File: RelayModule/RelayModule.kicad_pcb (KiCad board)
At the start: 2 copper layers, 49.9 x 21.3 mm, 16 parts, among them P1 Control_connector, P2 Power_connector, Q1 S8050, U1 PC817

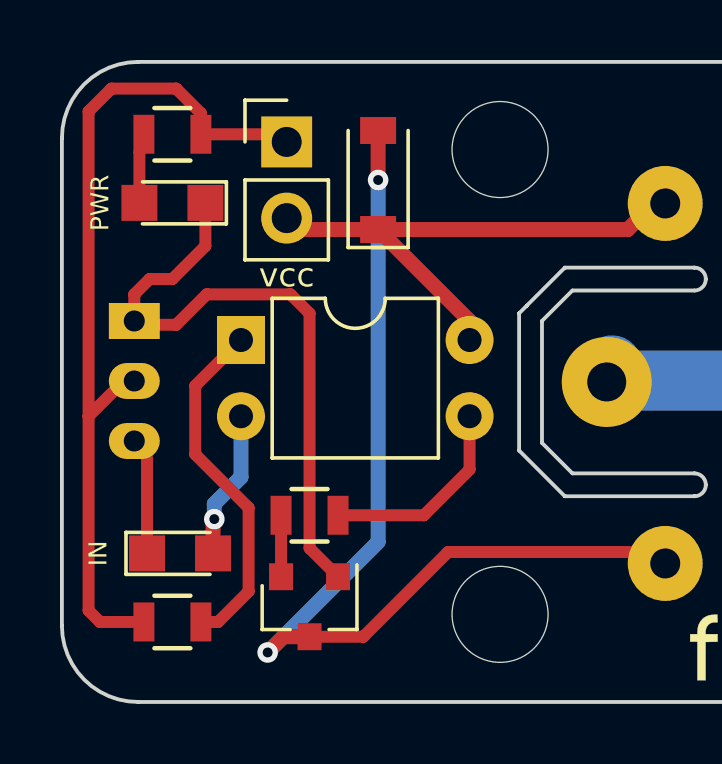
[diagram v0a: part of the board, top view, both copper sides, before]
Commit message: Solucionado un error en el footprint del transistor S8050
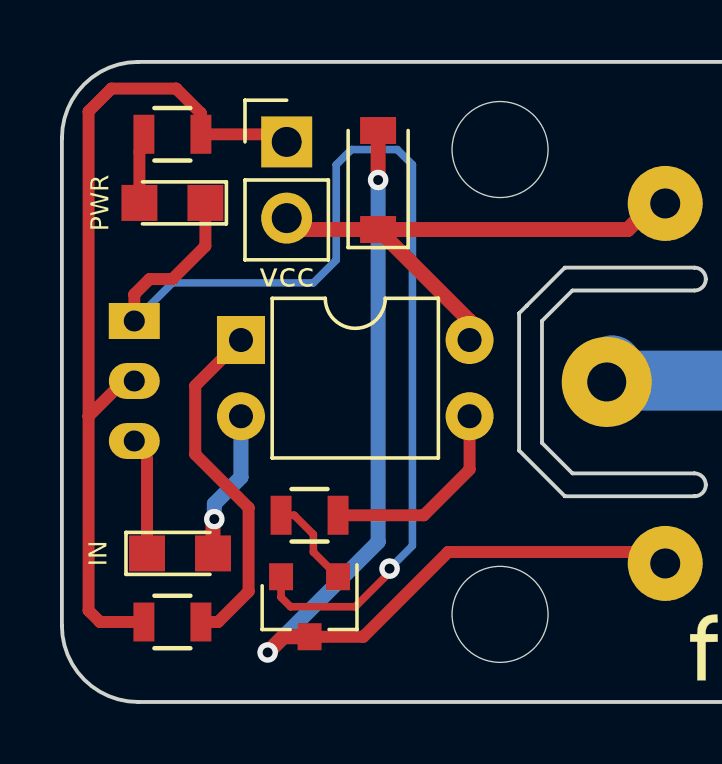
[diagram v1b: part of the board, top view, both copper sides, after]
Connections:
- Q1 pad 1: GND -> Net-(Q1-Pad1)
- Q1 pad 2: Net-(Q1-Pad2) -> GND
- R3 pad 1: Net-(Q1-Pad2) -> Net-(Q1-Pad1)
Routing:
- net GND: track 21.2 -> 38.0 mm, vias 0 -> 1
- net Net-(Q1-Pad1): track 0.00 -> 3.09 mm
- net Net-(Q1-Pad2): track 2.05 -> 0.00 mm
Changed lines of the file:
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@@
     (thickness 1.6)
     (drawings 29)
-    (tracks 67)
+    (tracks 79)
     (zones 0)
     (modules 16)
@@
   (net 9 "Net-(P2-Pad2)")
   (net 10 "Net-(P2-Pad3)")
-  (net 11 "Net-(Q1-Pad2)")
-  (net 12 "Net-(R2-Pad1)")
-  (net 13 "Net-(R3-Pad2)")
+  (net 11 "Net-(R2-Pad1)")
+  (net 12 "Net-(R3-Pad2)")
+  (net 13 "Net-(Q1-Pad1)")
   (net_class Default "Dit is de standaard class."
     (clearance 0.254)
@@
     (add_net "Net-(P2-Pad2)")
     (add_net "Net-(P2-Pad3)")
-    (add_net "Net-(Q1-Pad2)")
+    (add_net "Net-(Q1-Pad1)")
     (add_net "Net-(R2-Pad1)")
     (add_net "Net-(R3-Pad2)")
@@
     (fp_line (start 0.76 1.58) (end -0.7 1.58) (layer F.SilkS) (width 0.12))
     (pad 1 smd rect (at -1 -0.95 270) (size 0.9 0.8) (layers F.Cu F.Paste F.Mask)
+      (net 13 "Net-(Q1-Pad1)"))
+    (pad 2 smd rect (at -1 0.95 270) (size 0.9 0.8) (layers F.Cu F.Paste F.Mask)
       (net 2 GND))
-    (pad 2 smd rect (at -1 0.95 270) (size 0.9 0.8) (layers F.Cu F.Paste F.Mask)
-      (net 11 "Net-(Q1-Pad2)"))
     (pad 3 smd rect (at 1 0 270) (size 0.9 0.8) (layers F.Cu F.Paste F.Mask)
       (net 6 "Net-(D3-Pad2)"))
@@
     (fp_line (start -0.6 -0.875) (end 0.6 -0.875) (layer F.SilkS) (width 0.15))
     (pad 1 smd rect (at -0.95 0 180) (size 0.7 1.3) (layers F.Cu F.Paste F.Mask)
-      (net 12 "Net-(R2-Pad1)"))
+      (net 11 "Net-(R2-Pad1)"))
     (pad 2 smd rect (at 0.95 0 180) (size 0.7 1.3) (layers F.Cu F.Paste F.Mask)
       (net 7 VCC))
@@
     (fp_line (start -0.6 -0.875) (end 0.6 -0.875) (layer F.SilkS) (width 0.15))
     (pad 1 smd rect (at -0.95 0) (size 0.7 1.3) (layers F.Cu F.Paste F.Mask)
-      (net 11 "Net-(Q1-Pad2)"))
+      (net 13 "Net-(Q1-Pad1)"))
     (pad 2 smd rect (at 0.95 0) (size 0.7 1.3) (layers F.Cu F.Paste F.Mask)
-      (net 13 "Net-(R3-Pad2)"))
+      (net 12 "Net-(R3-Pad2)"))
     (model Resistors_SMD.3dshapes/R_0805.wrl
       (at (xyz 0 0 0))
@@
     (fp_line (start 8.7 -1.6) (end -1.1 -1.6) (layer F.CrtYd) (width 0.05))
     (pad 1 thru_hole rect (at 0 0) (size 1.6 1.6) (drill 0.8) (layers *.Cu *.Mask)
-      (net 12 "Net-(R2-Pad1)"))
+      (net 11 "Net-(R2-Pad1)"))
     (pad 3 thru_hole oval (at 7.62 2.54) (size 1.6 1.6) (drill 0.8) (layers *.Cu *.Mask)
-      (net 13 "Net-(R3-Pad2)"))
+      (net 12 "Net-(R3-Pad2)"))
     (pad 2 thru_hole oval (at 0 2.54) (size 1.6 1.6) (drill 0.8) (layers *.Cu *.Mask)
       (net 3 "Net-(D2-Pad2)"))
@@
   (segment (start 150.942 91.882) (end 150.792 92.032) (width 0.3) (layer F.Cu) (net 1))
   (segment (start 150.792 92.032) (end 150.792 93.726) (width 0.4) (layer F.Cu) (net 1))
-  (segment (start 150.622 97.79) (end 152.019 97.79) (width 0.4) (layer F.Cu) (net 2))
-  (segment (start 156.464 105.238) (end 157.414 106.188) (width 0.4) (layer F.Cu) (net 2))
-  (segment (start 156.464 97.409) (end 156.464 105.238) (width 0.4) (layer F.Cu) (net 2))
-  (segment (start 155.829 96.774) (end 156.464 97.409) (width 0.4) (layer F.Cu) (net 2))
-  (segment (start 153.035 96.774) (end 155.829 96.774) (width 0.4) (layer F.Cu) (net 2))
-  (segment (start 152.019 97.79) (end 153.035 96.774) (width 0.4) (layer F.Cu) (net 2))
+  (segment (start 155.514 106.188) (end 155.514 106.873) (width 0.254) (layer F.Cu) (net 2) (status 400000))
+  (segment (start 151.892 96.393) (end 150.622 97.663) (width 0.254) (layer B.Cu) (net 2) (status 800000))
+  (segment (start 156.591 96.393) (end 151.892 96.393) (width 0.254) (layer B.Cu) (net 2))
+  (segment (start 157.353 95.631) (end 156.591 96.393) (width 0.254) (layer B.Cu) (net 2))
+  (segment (start 157.353 92.456) (end 157.353 95.631) (width 0.254) (layer B.Cu) (net 2))
+  (segment (start 157.861 91.948) (end 157.353 92.456) (width 0.254) (layer B.Cu) (net 2))
+  (segment (start 159.385 91.948) (end 157.861 91.948) (width 0.254) (layer B.Cu) (net 2))
+  (segment (start 159.893 92.456) (end 159.385 91.948) (width 0.254) (layer B.Cu) (net 2))
+  (segment (start 159.893 105.156) (end 159.893 92.456) (width 0.254) (layer B.Cu) (net 2))
+  (segment (start 159.131 105.918) (end 159.893 105.156) (width 0.254) (layer B.Cu) (net 2))
+  (via (at 159.131 105.918) (size 0.6858) (drill 0.3302) (layers F.Cu B.Cu) (net 2))
+  (segment (start 159.131 106.045) (end 159.131 105.918) (width 0.254) (layer F.Cu) (net 2))
+  (segment (start 157.988 107.188) (end 159.131 106.045) (width 0.254) (layer F.Cu) (net 2))
+  (segment (start 155.829 107.188) (end 157.988 107.188) (width 0.254) (layer F.Cu) (net 2))
+  (segment (start 155.514 106.873) (end 155.829 107.188) (width 0.254) (layer F.Cu) (net 2))
   (segment (start 152.992 93.726) (end 152.992 95.166) (width 0.4) (layer F.Cu) (net 2))
   (segment (start 150.622 96.774) (end 150.622 97.79) (width 0.4) (layer F.Cu) (net 2))
@@
   (segment (start 189.992 94.64802) (end 181.52302 94.64802) (width 2) (layer B.Cu) (net 10))
   (segment (start 181.52302 94.64802) (end 180.57 93.695) (width 2) (layer B.Cu) (net 10))
-  (segment (start 155.514 106.188) (end 155.514 104.14) (width 0.4) (layer F.Cu) (net 11))
-  (segment (start 152.842 107.696) (end 153.416 107.696) (width 0.4) (layer F.Cu) (net 12))
-  (segment (start 152.654 99.822) (end 154.178 98.298) (width 0.4) (layer F.Cu) (net 12))
-  (segment (start 152.654 102.108) (end 152.654 99.822) (width 0.4) (layer F.Cu) (net 12))
-  (segment (start 154.432 103.886) (end 152.654 102.108) (width 0.4) (layer F.Cu) (net 12))
-  (segment (start 154.432 106.68) (end 154.432 103.886) (width 0.4) (layer F.Cu) (net 12))
-  (segment (start 153.416 107.696) (end 154.432 106.68) (width 0.4) (layer F.Cu) (net 12))
-  (segment (start 157.414 104.14) (end 160.274 104.14) (width 0.4) (layer F.Cu) (net 13))
-  (segment (start 161.798 102.616) (end 161.798 100.838) (width 0.4) (layer F.Cu) (net 13))
-  (segment (start 160.274 104.14) (end 161.798 102.616) (width 0.4) (layer F.Cu) (net 13))
+  (segment (start 152.842 107.696) (end 153.416 107.696) (width 0.4) (layer F.Cu) (net 11))
+  (segment (start 152.654 99.822) (end 154.178 98.298) (width 0.4) (layer F.Cu) (net 11))
+  (segment (start 152.654 102.108) (end 152.654 99.822) (width 0.4) (layer F.Cu) (net 11))
+  (segment (start 154.432 103.886) (end 152.654 102.108) (width 0.4) (layer F.Cu) (net 11))
+  (segment (start 154.432 106.68) (end 154.432 103.886) (width 0.4) (layer F.Cu) (net 11))
+  (segment (start 153.416 107.696) (end 154.432 106.68) (width 0.4) (layer F.Cu) (net 11))
+  (segment (start 157.414 104.14) (end 160.274 104.14) (width 0.4) (layer F.Cu) (net 12))
+  (segment (start 161.798 102.616) (end 161.798 100.838) (width 0.4) (layer F.Cu) (net 12))
+  (segment (start 160.274 104.14) (end 161.798 102.616) (width 0.4) (layer F.Cu) (net 12))
+  (segment (start 155.514 104.14) (end 155.956 104.14) (width 0.254) (layer F.Cu) (net 13) (status 400000))
+  (segment (start 156.591 105.365) (end 157.414 106.188) (width 0.254) (layer F.Cu) (net 13) (status 800000))
+  (segment (start 156.591 104.775) (end 156.591 105.365) (width 0.254) (layer F.Cu) (net 13))
+  (segment (start 155.956 104.14) (end 156.591 104.775) (width 0.254) (layer F.Cu) (net 13))
 )
